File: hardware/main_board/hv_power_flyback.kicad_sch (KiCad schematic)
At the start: 28 parts, among them Q19 FDS2734, U8 LM5155

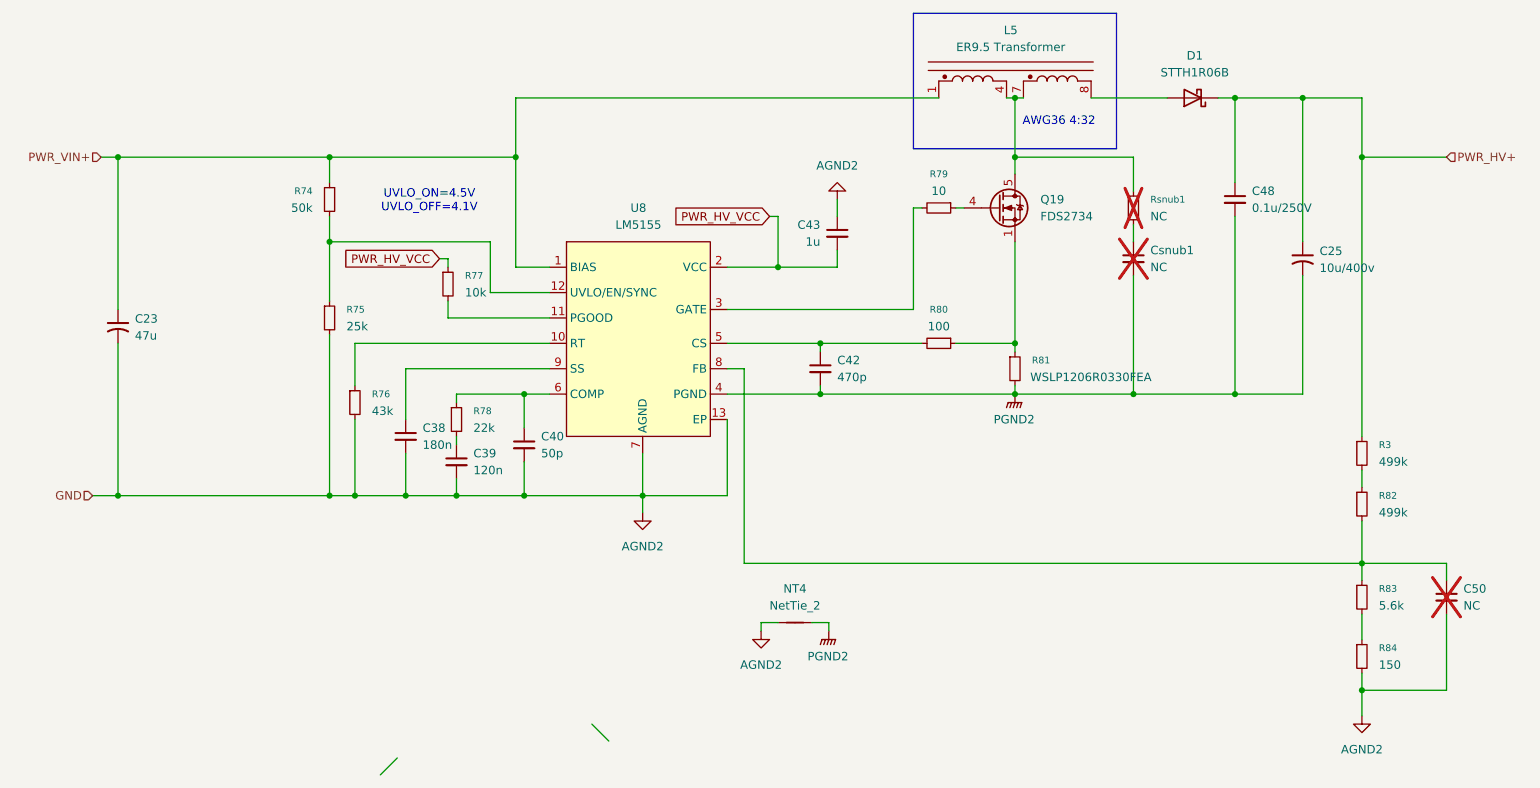
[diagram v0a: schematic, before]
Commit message: hardware(sch): update component package to 0402 as most as possable, layout is still need to complete
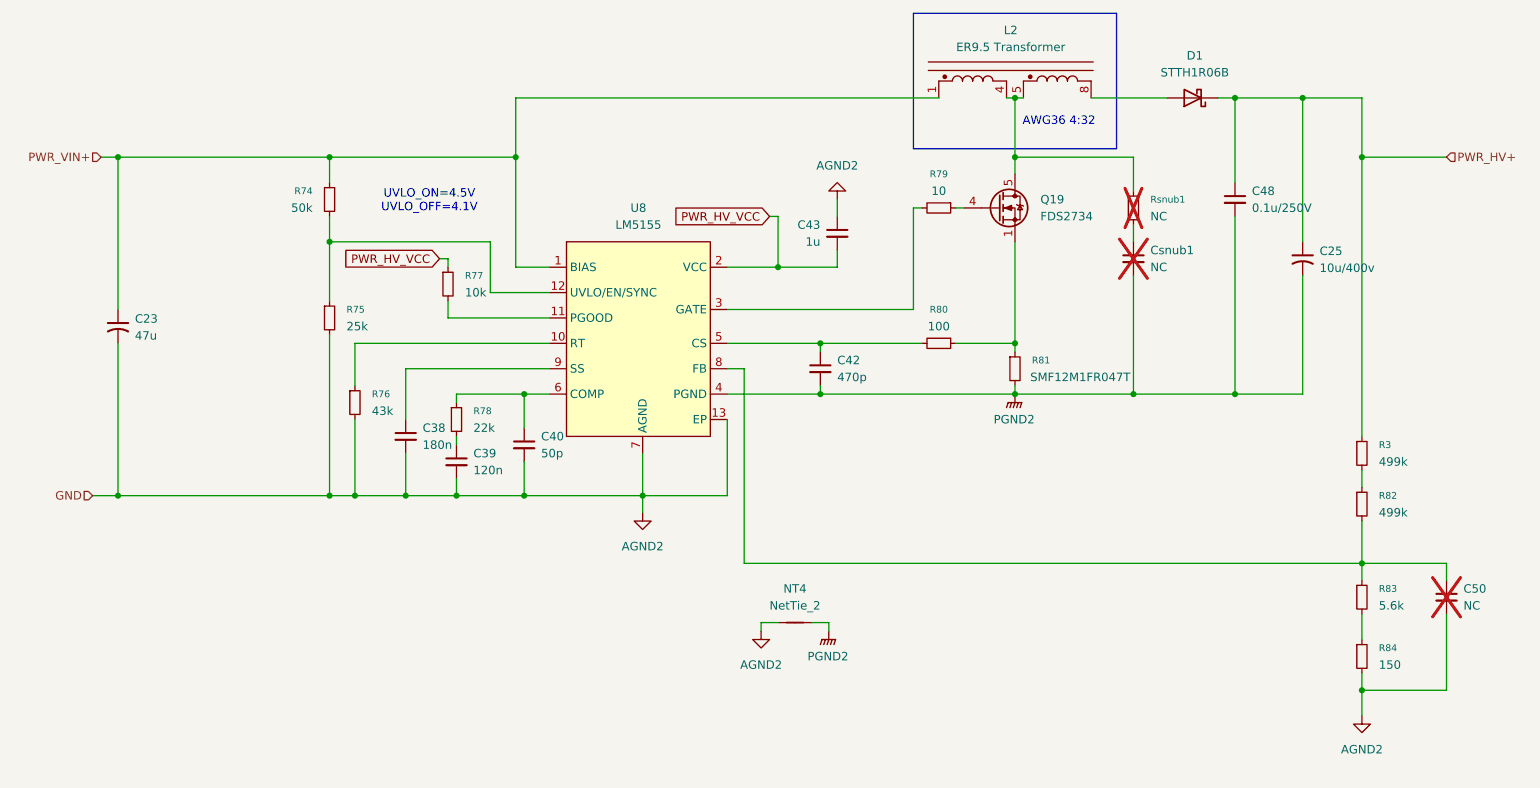
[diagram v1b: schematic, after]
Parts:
- removed L5: ER9.5 Transformer, KiCad_Library:Transformer_ER9.5_11.6mmx8.2mm, symbol Johnson_Symbol_Lib:ER9.5_auto_transformer
- added L2: ER9.5 Transformer, KiCad_Library:Transformer_ER9.5_11.6mmx8.2mm, symbol Johnson_Symbol_Lib:ER9.5_auto_transformer
- C25: now left out of the parts list
- R81: value WSLP1206R0330FEA -> SMF12M1FR047T; LCSC PN C2084257 -> C845295
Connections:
- net PWR_VIN+: now also L2.1
- net at D1.2 (A): now also L2.8
- net at Q19.5 (D), Q19.6 (D), Q19.7 (D)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: now also L2.4, L2.5
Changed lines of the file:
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@@
 		(color 0 0 0 0)
 	)
-	(bus_entry
-		(at 119.38 124.46)
-		(size 2.54 2.54)
-		(stroke
-			(width 0)
-			(type default)
-		)
-	)
-	(bus_entry
-		(at 90.17 129.54)
-		(size -2.54 2.54)
-		(stroke
-			(width 0)
-			(type default)
-		)
-	)
 	(wire
 		(pts
@@
 			)
 		)
-		(property "Value" "WSLP1206R0330FEA"
+		(property "Value" "SMF12M1FR047T"
 			(at 185.166 72.39 0)
 			(effects
@@
 			)
 		)
-		(property "Description" "Resistor, small symbol"
+		(property "Description" "1W 47mΩ Current Sense Resistor SMD ±1% ±50ppm/℃"
 			(at 196.342 76.962 0)
 			(effects
@@
 			)
 		)
-		(property "LCSC PN" "C2084257"
+		(property "LCSC PN" "C845295"
 			(at 182.88 71.12 0)
 			(effects
@@
 		(unit 1)
 		(exclude_from_sim no)
-		(in_bom yes)
+		(in_bom no)
 		(on_board yes)
 		(dnp no)
@@
 	)
 	(symbol
-		(lib_id "Johnson_Symbol_Lib:ER9.5_auto_transformer")
-		(at 181.61 40.64 0)
+		(lib_id "Device:R_Small")
+		(at 80.01 45.72 0)
+		(mirror y)
 		(unit 1)
 		(exclude_from_sim no)
@@
 		(on_board yes)
 		(dnp no)
-		(fields_autoplaced yes)
-		(property "Reference" "L5"
-			(at 182.245 20.32 0)
+		(property "Reference" "R74"
+			(at 77.47 44.4499 0)
 			(effects
 				(font
-					(size 1.27 1.27)
+					(size 1.016 1.016)
 				)
+				(justify left)
 			)
 		)
-		(property "Value" "ER9.5 Transformer"
-			(at 182.245 22.86 0)
+		(property "Value" "50k"
+			(at 77.47 46.9899 0)
 			(effects
 				(font
 					(size 1.27 1.27)
 				)
+				(justify left)
 			)
 		)
-		(property "Footprint" "KiCad_Library:Transformer_ER9.5_11.6mmx8.2mm"
-			(at 181.61 40.64 0)
+		(property "Footprint" "Resistor_SMD:R_0603_1608Metric"
+			(at 80.01 45.72 0)
 			(effects
 				(font
@@
 			)
 		)
-		(property "Datasheet" "https://www.tdk-electronics.tdk.com/inf/80/db/fer/er_9_5_5.pdf"
-			(at 181.61 40.64 0)
+		(property "Datasheet" "~"
+			(at 80.01 45.72 0)
 			(effects
 				(font
@@
 			)
 		)
-		(property "Description" "ER9.5 boost autotransformer"
-			(at 181.61 40.64 0)
+		(property "Description" "Resistor, small symbol"
+			(at 80.01 45.72 0)
 			(effects
 				(font
@@
 			)
 		)
-		(property "Digikey PN" "B65527B1008T001"
-			(at 181.864 43.434 0)
+		(property "LCSC PN" "C304067"
+			(at 80.01 45.72 0)
 			(effects
 				(font
@@
 			)
 		)
-		(pin "7"
-		)
-		(pin "8"
+		(pin "2"
 		)
 		(pin "1"
 		)
-		(pin "4"
-		)
 		(instances
-			(project ""
+			(project "main_board"
 				(path "/62950e93-3f98-4dee-9256-8213caa98ee7/ac187de9-7d82-4fdd-b064-4ef8ee34b2fe"
-					(reference "L5")
+					(reference "R74")
 					(unit 1)
 				)
@@
 	(symbol
 		(lib_id "Device:R_Small")
-		(at 80.01 45.72 0)
-		(mirror y)
+		(at 171.45 46.99 270)
 		(unit 1)
 		(exclude_from_sim no)
@@
 		(on_board yes)
 		(dnp no)
-		(property "Reference" "R74"
-			(at 77.47 44.4499 0)
+		(fields_autoplaced yes)
+		(property "Reference" "R79"
+			(at 171.45 41.91 90)
 			(effects
 				(font
 					(size 1.016 1.016)
 				)
-				(justify left)
 			)
 		)
-		(property "Value" "50k"
-			(at 77.47 46.9899 0)
+		(property "Value" "10"
+			(at 171.45 44.45 90)
 			(effects
 				(font
 					(size 1.27 1.27)
 				)
-				(justify left)
 			)
 		)
 		(property "Footprint" "Resistor_SMD:R_0603_1608Metric"
-			(at 80.01 45.72 0)
+			(at 171.45 46.99 0)
 			(effects
 				(font
@@
 		)
 		(property "Datasheet" "~"
-			(at 80.01 45.72 0)
+			(at 171.45 46.99 0)
 			(effects
 				(font
@@
 		)
 		(property "Description" "Resistor, small symbol"
-			(at 80.01 45.72 0)
+			(at 171.45 46.99 0)
 			(effects
 				(font
@@
 			)
 		)
-		(property "LCSC PN" "C304067"
-			(at 80.01 45.72 0)
+		(property "LCSC PN" "C22859"
+			(at 171.45 46.99 0)
 			(effects
 				(font
@@
 			(project "main_board"
 				(path "/62950e93-3f98-4dee-9256-8213caa98ee7/ac187de9-7d82-4fdd-b064-4ef8ee34b2fe"
-					(reference "R74")
+					(reference "R79")
 					(unit 1)
 				)
@@
 	)
 	(symbol
-		(lib_id "Device:R_Small")
-		(at 171.45 46.99 270)
+		(lib_id "Johnson_Symbol_Lib:ER9.5_auto_transformer")
+		(at 181.61 40.64 0)
 		(unit 1)
 		(exclude_from_sim no)
-		(in_bom yes)
+		(in_bom no)
 		(on_board yes)
 		(dnp no)
 		(fields_autoplaced yes)
-		(property "Reference" "R79"
-			(at 171.45 41.91 90)
+		(property "Reference" "L2"
+			(at 182.245 20.32 0)
 			(effects
 				(font
-					(size 1.016 1.016)
+					(size 1.27 1.27)
 				)
 			)
 		)
-		(property "Value" "10"
-			(at 171.45 44.45 90)
+		(property "Value" "ER9.5 Transformer"
+			(at 182.245 22.86 0)
 			(effects
 				(font
@@
 			)
 		)
-		(property "Footprint" "Resistor_SMD:R_0603_1608Metric"
-			(at 171.45 46.99 0)
+		(property "Footprint" "KiCad_Library:Transformer_ER9.5_11.6mmx8.2mm"
+			(at 181.61 40.64 0)
 			(effects
 				(font
@@
 			)
 		)
-		(property "Datasheet" "~"
-			(at 171.45 46.99 0)
+		(property "Datasheet" "https://www.tdk-electronics.tdk.com/inf/80/db/fer/er_9_5_5.pdf"
+			(at 181.61 40.64 0)
 			(effects
 				(font
@@
 			)
 		)
-		(property "Description" "Resistor, small symbol"
-			(at 171.45 46.99 0)
+		(property "Description" "ER9.5 boost autotransformer"
+			(at 181.61 40.64 0)
 			(effects
 				(font
@@
 			)
 		)
-		(property "LCSC PN" "C22859"
-			(at 171.45 46.99 0)
+		(property "Digikey PN" "B65527B1008T001"
+			(at 181.864 43.434 0)
 			(effects
 				(font
@@
 			)
 		)
-		(pin "2"
+		(pin "8"
+		)
+		(pin "5"
 		)
 		(pin "1"
 		)
+		(pin "4"
+		)
 		(instances
-			(project "main_board"
+			(project ""
 				(path "/62950e93-3f98-4dee-9256-8213caa98ee7/ac187de9-7d82-4fdd-b064-4ef8ee34b2fe"
-					(reference "R79")
+					(reference "L2")
 					(unit 1)
 				)
